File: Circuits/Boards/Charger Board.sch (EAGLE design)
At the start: 0 parts

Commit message: 
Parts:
- added B1: PIEZOBUZZER, Passive:PIEZOBUZZER
- added C1, C3, C8, C9: 1uf, Passive:CAP0603
- added C2, C6, C7: 10uf, Passive:CAP0805
- added C4, C5: 4.7uf, Passive:CAP0603
- added CON1: ISP(2X3), Mechanical:ISP(2X3)
- added CON2: FTDI(1X6), Mechanical:FTDI(1X6)
- added LED1, LED10, LED8, LED9: (no value), Passive:LED0603
- added LED13, LED2, LED3, LED4, LED5, LED6, LED7: IR, Passive:LED5MMRA
- added PR1: 500k-20k, Passive:CDSPHOTORESISTOR
- added R1: 2k, Passive:RES0603
- added R10, R11, R12, R13, R14, R15, R17, R18, R19, R20, R21, R22, R24, R25, R26, R27, R28: (no value), Passive:RES0603
- added R16, R23: 500, Passive:RES0603
- added R2: 1.5k, Passive:RES0603
- added R3: 400, Passive:RES0603
- added R4: 600, Passive:RES0603
- added R5, R7: 10k, Passive:RES0603
- added R6: 15k, Passive:RES0603
- added R8: 1k, Passive:RES0603
- added R9: 20k, Passive:RES0603
- added T1, T2, T3: NPN2N2222, Passive:NPN2N2222
- added T4, T5, T6, T7, T8, T9: TEFT4300, Passive:TEFT4300
- added U1: ATMEGA324P, DigitalIC:ATMEGA324P
- added U2: MCP73832SOT-23, PowerIC:MCP73832SOT-23
- added U3: TB6552FN/FNG, DigitalIC:TB6552FN/FNG
- added V1: MCP1700-3002E, PowerIC:MCP1700-3002E
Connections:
- new net +3V: B1.+, C2.1, C3.1, C6.1, C7.1, C8.1, LED13.A, LED2.A, LED3.A, LED4.A, LED5.A, LED6.A, LED7.A, LED9.A, PR1.2, R7.1, R8.2, T4.C, T5.C, T6.C, T7.C, T8.C, T9.C, U1.AREF, U1.AVCC, U1.VCC, U3.VCC, V1.OUT
- new net +VBAT: C1.1, C4.1, C9.1, R5.2, U2.VBAT, U3.VM, V1.IN
- new net +VCHG: C5.1, R2.2, R3.2, U2.VDD
- new net AIN1: U3.AIN1
- new net AIN2: U3.AIN2
- new net APWM: U3.APWM
- new net BIN1: U3.BIN1
- new net BIN2: U3.BIN2
- new net BPWM: U3.BPWM
- new net BUZZER: R28.1
- new net CHGDETECT: R3.1, R4.2
- new net CHGSTATUS: LED1.C, U2.STAT
- new net DISTANCELED: R23.1
- new net GND: C1.2, C2.2, C3.2, C4.2, C5.2, C6.2, C7.2, C8.2, CON1.GND, CON2.GND, R1.1, R17.1, R18.1, R19.1, R20.1, R21.1, R24.1, R4.1, R6.1, R9.1, T1.E, T2.E, T3.E, U1.GND, U2.VSS, U3.GND, U3.PGND, V1.GND
- new net LED1: R25.1
- new net LED2: R26.1
- new net LED3: R27.1
- new net LIGHTSENSE: PR1.1, R9.2, U1.PA1(ADC1/PCINT1)
- new net LINESENSE1: U1.PA2(ADC2/PCINT2)
- new net LINESENSE2: U1.PA3(ADC3/PCINT3)
- new net MA+: U3.AO1
- new net MA-: U3.AO2
- new net MB+: U3.BO1
- new net MB-: U3.BO2
- new net N$1: R1.2, U2.PROG
- new net N$10: R10.1, R11.1, R12.1, R13.1, R14.1, R15.1, T2.C
- new net N$11: R16.2, T2.B
- new net N$12: R22.1, T3.C
- new net N$13: LED2.C, R10.2
- new net N$14: LED3.C, R11.2
- new net N$15: LED4.C, R12.2
- new net N$16: LED5.C, R13.2
- new net N$17: LED6.C, R14.2
- new net N$18: LED7.C, R15.2
- new net N$19: R23.2, T3.B
- new net N$2: CON1.MOSI, U1.PB5(PCINT13/MOSI)
- new net N$20: LED8.C, R25.2
- new net N$21: LED9.C, R26.2
- new net N$22: LED10.C, R27.2
- new net N$23: C9.2
- new net N$24: LED10.A, LED8.A
- new net N$25: LED13.C, R22.2
- new net N$26: R28.2, T1.B
- new net N$3: CON1.MISO, U1.PB6(PCINT14/MISO)
- new net N$4: LED1.A, R2.1
- new net N$5: CON1.SCK, U1.PB7(PCINT15/SCK)
- new net N$6: CON1.!RESET, R7.2, U1.!RESET
- new net N$7: CON2.RXI, U1.PD1(PCINT25/TXD0)
- new net N$8: CON2.TXO, U1.PD0(PCINT24/RXD0)
- new net N$9: B1.-, R8.1, T1.C
- new net R_A: R17.2, T4.E
- new net R_D: R18.2, R19.2, R20.2, R21.2, R24.2, T5.E, T6.E, T7.E, T8.E, T9.E
- new net STBY: U3.ASTBY, U3.BSTBY
- new net TRANSMITLEDS: R16.1
- new net VSENSE: R5.1, R6.2, U1.PA0(ADC0/PCINT0)
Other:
- note added: "4.6v ideal"

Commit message: 
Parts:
- removed C1, C8, C9: 1uf, Passive:CAP0603
- removed C2, C7: 10uf, Passive:CAP0805
- removed C4, C5: 4.7uf, Passive:CAP0603
- removed LED1: (no value), Passive:LED0603
- removed LED13: IR, Passive:LED5MMRA
- removed PR1: 500k-20k, Passive:CDSPHOTORESISTOR
- removed R1: 2k, Passive:RES0603
- removed R2: 1.5k, Passive:RES0603
- removed R22: (no value), Passive:RES0603
- removed R23: 500, Passive:RES0603
- removed R3: 400, Passive:RES0603
- removed R4: 600, Passive:RES0603
- removed R5: 10k, Passive:RES0603
- removed R6: 15k, Passive:RES0603
- removed R9: 20k, Passive:RES0603
- removed T3: NPN2N2222, Passive:NPN2N2222
- removed U2: MCP73832SOT-23, PowerIC:MCP73832SOT-23
- removed U3: TB6552FN/FNG, DigitalIC:TB6552FN/FNG
- removed V1: MCP1700-3002E, PowerIC:MCP1700-3002E
- added CON3: CHARGERCONTACTS, Mechanical:CHARGERCONTACTS
- added S1: ROCKER_SWITCH, Mechanical:ROCKER_SWITCH
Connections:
- removed net +VBAT: C1.1, C4.1, C9.1, R5.2, U2.VBAT, U3.VM, V1.IN
- removed net +VCHG: C5.1, R2.2, R3.2, U2.VDD
- removed net AIN1: U3.AIN1
- removed net AIN2: U3.AIN2
- removed net APWM: U3.APWM
- removed net BIN1: U3.BIN1
- removed net BIN2: U3.BIN2
- removed net BPWM: U3.BPWM
- removed net CHGDETECT: R3.1, R4.2
- removed net CHGSTATUS: LED1.C, U2.STAT
- removed net DISTANCELED: R23.1
- removed net LIGHTSENSE: PR1.1, R9.2, U1.PA1(ADC1/PCINT1)
- removed net LINESENSE1: U1.PA2(ADC2/PCINT2)
- removed net LINESENSE2: U1.PA3(ADC3/PCINT3)
- removed net MA+: U3.AO1
- removed net MA-: U3.AO2
- removed net MB+: U3.BO1
- removed net MB-: U3.BO2
- removed net N$1: R1.2, U2.PROG
- removed net N$12: R22.1, T3.C
- removed net N$19: R23.2, T3.B
- removed net N$23: C9.2
- removed net N$25: LED13.C, R22.2
- removed net STBY: U3.ASTBY, U3.BSTBY
- removed net VSENSE: R5.1, R6.2, U1.PA0(ADC0/PCINT0)
- new net +5V: B1.+, C3.1, C6.1, LED2.A, LED3.A, LED4.A, LED5.A, LED6.A, LED7.A, LED9.A, R8.2, S1.2, T4.C, T5.C, T6.C, T7.C, T8.C, T9.C, U1.AREF, U1.AVCC, U1.VCC
- new net CURRENTSENSE: U1.PA0(ADC0/PCINT0)
- new net VIN: S1.1
- net +3V: no longer B1.+, C2.1, C3.1, C6.1, C7.1, C8.1, LED13.A, LED2.A, LED3.A, LED4.A, LED5.A, LED6.A, LED7.A, LED9.A, PR1.2, R8.2, T4.C, T5.C, T6.C, T7.C, T8.C, T9.C, U1.AREF, U1.AVCC, U1.VCC, U3.VCC, V1.OUT
- net GND: now also CON3.GND; no longer C1.2, C2.2, C4.2, C5.2, C7.2, C8.2, R1.1, R4.1, R6.1, R9.1, T3.E, U2.VSS, U3.GND, U3.PGND, V1.GND
- net N$4: now also CON3.+V; no longer LED1.A, R2.1
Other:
- note removed: "4.6v ideal"
- moved on the sheet: C6, LED2, LED3, LED4, LED5, LED6, LED7, R10, R11, R12, R13, R14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

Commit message: updated charger schematic, and added swarm board board file
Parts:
- added C1: .1uf, Passive:CAP0603
- added C2: 1nf, Passive:CAP0603
- added R1: 1k, Passive:RES0603
- added T3: IRF7416PBF, Passive:IRF7416PBF
- added U2: ACS711, PowerIC:ACS711
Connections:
- removed net +3V: R7.1
- new net +VCHG: B1.+, C1.1, C3.1, LED9.A, R7.1, R8.2, S1.2, T3.S, U1.AREF, U1.AVCC, U1.VCC, U2.VCC
- new net CHARGER: T3.G, U1.PB0(XCK0/T0/PCINT8)
- new net N$1: T3.D, U2.IP+
- new net N$12: C2.1, R1.1, U2.VIOUT
- net +5V: no longer B1.+, C3.1, LED9.A, R8.2, S1.2, U1.AREF, U1.AVCC, U1.VCC
- net CURRENTSENSE: now also R1.2
- net GND: now also C2.2, U2.GND
- net N$4: now also U2.IP-
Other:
- note added: "These go to the charger contacts"

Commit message: Large updates to the charger board
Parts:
- added C4: .1uf, Passive:CAP0603
- added C5: 1uf, Passive:CAP0603
- added D1, D2: PMEG3050EP, Passive:PMEG3050EP
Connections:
- removed net N$4: CON3.+V, U2.IP-
- new net N$19: CON3.+V, D1.C, D2.C
- new net N$23: D1.A, D2.A, U2.IP-
- net +5V: now also B1.+, C1.1, C3.1, C4.1, C5.1, LED9.A, R8.2, S1.2, T3.S, U1.AREF, U1.AVCC, U1.VCC, U2.VCC
- net +VCHG: no longer B1.+, C1.1, C3.1, LED9.A, R8.2, S1.2, T3.S, U1.AREF, U1.AVCC, U1.VCC, U2.VCC
- net GND: now also C1.2, C4.2, C5.2
- net LED1: now also U1.PB1(T1/CLKO/PCINT9)
- net LED2: now also U1.PB2(AIN0/INT2/PCINT10)
- net LED3: now also U1.PB3(AIN1/OC0A/PCINT11)
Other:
- moved on the sheet: B1, C1, C2, LED10, LED8, LED9, R1, R25, R26, R27, R28, R8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

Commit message: updates to both boards and libraries. Added hall effect sensors to charger board
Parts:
- added U10, U3, U4, U5, U6, U7, U8, U9: HALLEFFECT, DigitalIC:HALLEFFECT
- R25, R26, R27: value (none) -> 200
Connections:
- new net BAY1: U1.PC0(PCINT16/SCL), U3.!VOUT
- new net BAY2: U1.PC1(PCINT17/SDA), U4.!VOUT
- new net BAY3: U1.PC2(PCINT18/TCK), U5.!VOUT
- new net BAY4: U1.PC3(PCINT19/TMS), U6.!VOUT
- new net BAY5: U1.PC4(TDO/PCINT20), U7.!VOUT
- new net BAY6: U1.PC5(TDI/PCINT21), U8.!VOUT
- new net BAY7: U1.PC6(TOSC1/PCINT22), U9.!VOUT
- new net BAY8: U1.PC7(TOSC2/PCINT23), U10.!VOUT
- net +5V: now also U10.VCC, U3.VCC, U4.VCC, U5.VCC, U6.VCC, U7.VCC, U8.VCC, U9.VCC
- net GND: now also U10.GND, U3.GND, U4.GND, U5.GND, U6.GND, U7.GND, U8.GND, U9.GND
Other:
- moved on the sheet: C6, CON2, LED2, LED3, LED4, LED5, LED6, LED7, R10, R11, R12, R13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

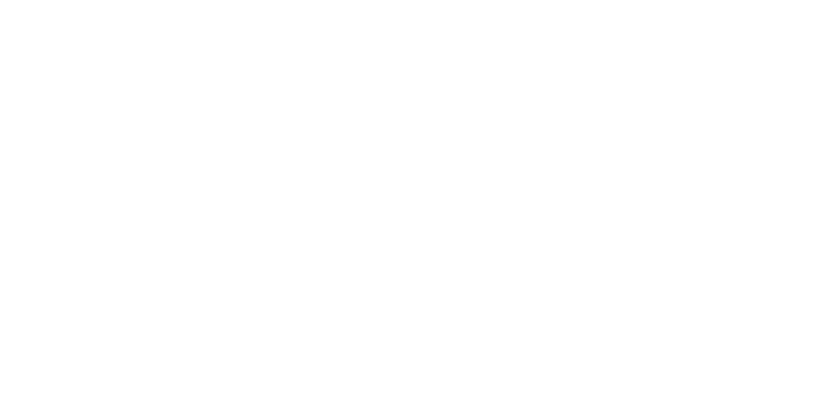
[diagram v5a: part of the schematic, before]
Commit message: 
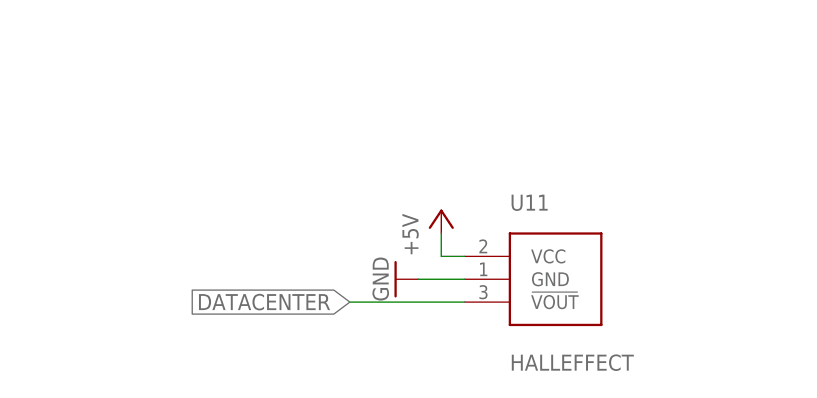
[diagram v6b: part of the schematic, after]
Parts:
- added U11: HALLEFFECT, DigitalIC:HALLEFFECT
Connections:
- new net DATACENTER: U11.!VOUT
- net +5V: now also U11.VCC
- net GND: now also U11.GND
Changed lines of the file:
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@@
 <part name="P+17" library="Supply" deviceset="+5V" device=""/>
 <part name="U10" library="DigitalIC" deviceset="HALLEFFECT" device=""/>
+<part name="GND24" library="Supply" deviceset="GND" device=""/>
+<part name="P+18" library="Supply" deviceset="+5V" device=""/>
+<part name="U11" library="DigitalIC" deviceset="HALLEFFECT" device=""/>
 </parts>
 <sheets>
@@
 <instance part="P+17" gate="1" x="162.56" y="-106.68"/>
 <instance part="U10" gate="G$1" x="175.26" y="-114.3"/>
+<instance part="GND24" gate="1" x="154.94" y="-162.56" rot="R270"/>
+<instance part="P+18" gate="1" x="160.02" y="-154.94"/>
+<instance part="U11" gate="G$1" x="172.72" y="-162.56"/>
 </instances>
 <busses>
@@
 <pinref part="GND23" gate="1" pin="GND"/>
 <pinref part="U10" gate="G$1" pin="GND"/>
+</segment>
+<segment>
+<wire x1="162.56" y1="-162.56" x2="157.48" y2="-162.56" width="0.1524" layer="91"/>
+<pinref part="GND24" gate="1" pin="GND"/>
+<pinref part="U11" gate="G$1" pin="GND"/>
 </segment>
 </net>
@@
 <pinref part="U10" gate="G$1" pin="VCC"/>
 </segment>
+<segment>
+<wire x1="162.56" y1="-160.02" x2="160.02" y2="-160.02" width="0.1524" layer="91"/>
+<wire x1="160.02" y1="-160.02" x2="160.02" y2="-157.48" width="0.1524" layer="91"/>
+<pinref part="P+18" gate="1" pin="+5V"/>
+<pinref part="U11" gate="G$1" pin="VCC"/>
+</segment>
 </net>
 <net name="VIN" class="0">
@@
 </segment>
 </net>
+<net name="DATACENTER" class="0">
+<segment>
+<wire x1="162.56" y1="-165.1" x2="149.86" y2="-165.1" width="0.1524" layer="91"/>
+<label x="149.86" y="-165.1" size="1.778" layer="91" rot="R180" xref="yes"/>
+<pinref part="U11" gate="G$1" pin="!VOUT"/>
+</segment>
+</net>

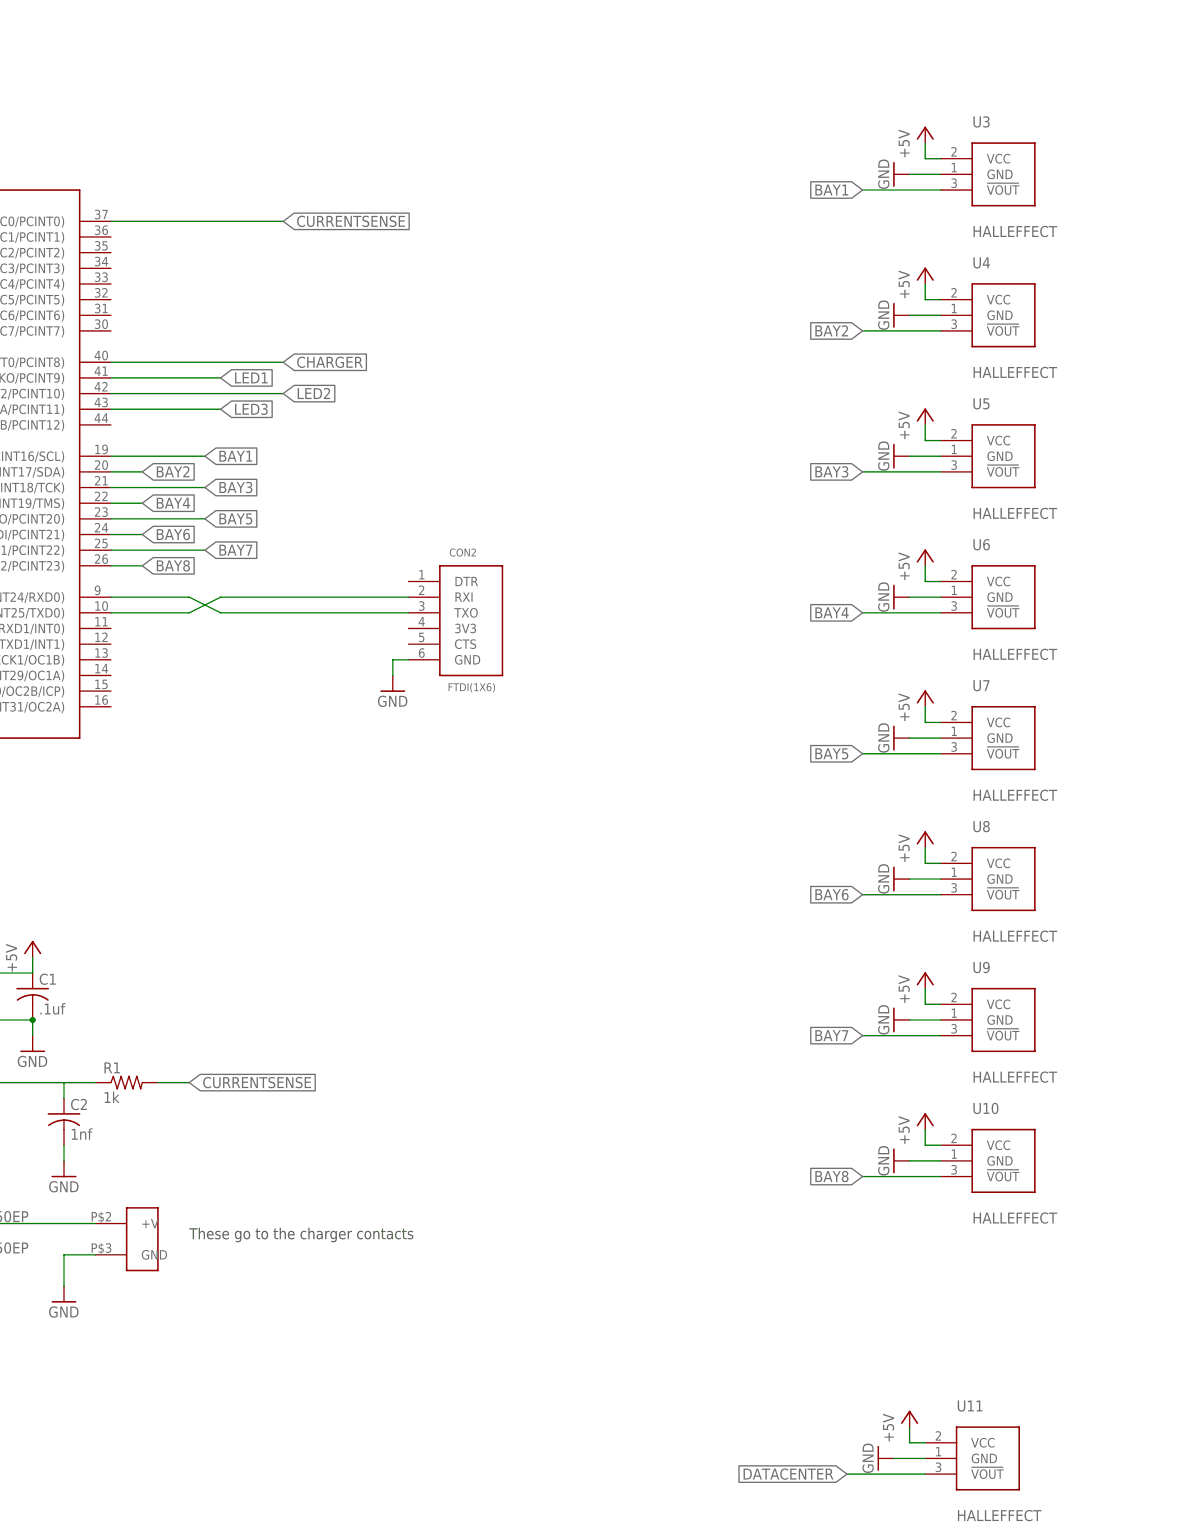
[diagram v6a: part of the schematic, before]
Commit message: 
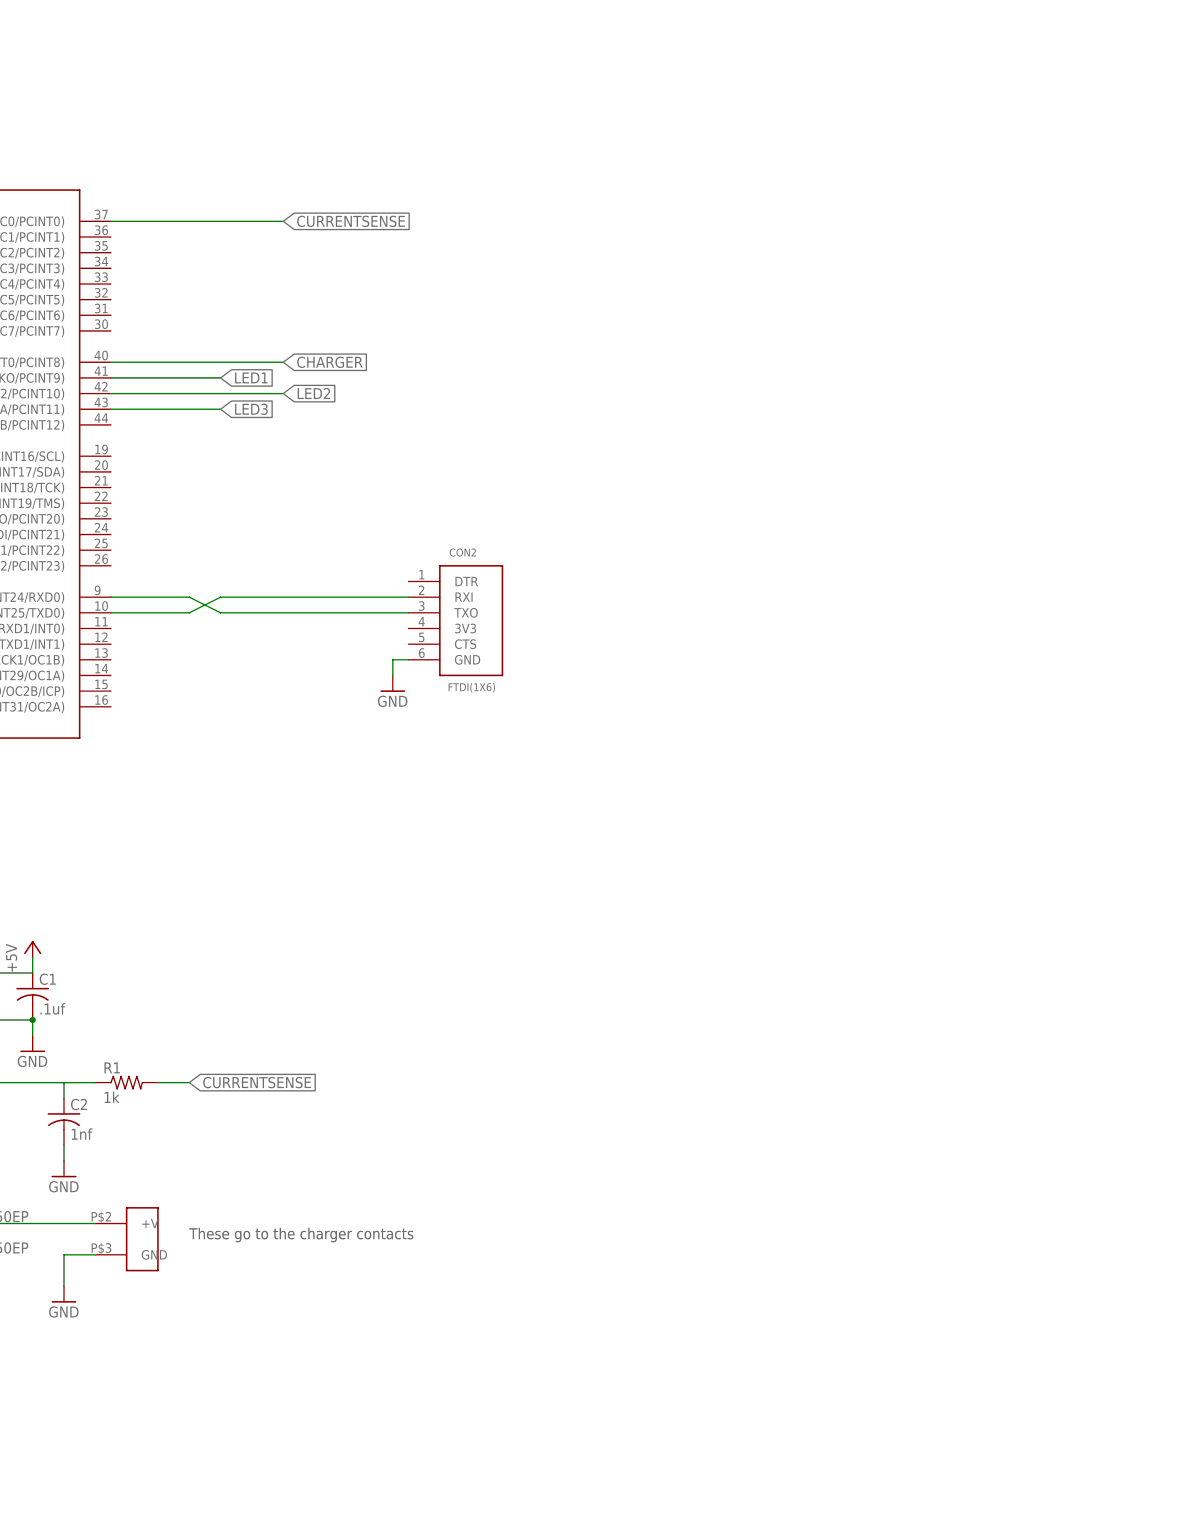
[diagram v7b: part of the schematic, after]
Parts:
- removed U10, U11, U3, U4, U5, U6, U7, U8, U9: HALLEFFECT, DigitalIC:HALLEFFECT
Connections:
- removed net BAY1: U1.PC0(PCINT16/SCL), U3.!VOUT
- removed net BAY2: U1.PC1(PCINT17/SDA), U4.!VOUT
- removed net BAY3: U1.PC2(PCINT18/TCK), U5.!VOUT
- removed net BAY4: U1.PC3(PCINT19/TMS), U6.!VOUT
- removed net BAY5: U1.PC4(TDO/PCINT20), U7.!VOUT
- removed net BAY6: U1.PC5(TDI/PCINT21), U8.!VOUT
- removed net BAY7: U1.PC6(TOSC1/PCINT22), U9.!VOUT
- removed net BAY8: U1.PC7(TOSC2/PCINT23), U10.!VOUT
- removed net DATACENTER: U11.!VOUT
- net +5V: no longer U10.VCC, U11.VCC, U3.VCC, U4.VCC, U5.VCC, U6.VCC, U7.VCC, U8.VCC, U9.VCC
- net GND: no longer U10.GND, U11.GND, U3.GND, U4.GND, U5.GND, U6.GND, U7.GND, U8.GND, U9.GND

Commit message: updated libraries and charger board
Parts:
- removed CON2: FTDI(1X6), Mechanical:FTDI(1X6)
- removed D1, D2: PMEG3050EP, Passive:PMEG3050EP
- removed R21, R24: (no value), Passive:RES0603
- removed T4, T5, T6, T7, T8, T9: TEFT4300, Passive:TEFT4300
- added CON10, CON11, CON12, CON4, CON5, CON6, CON7, CON8, CON9: HEADER_3X1, Mechanical:HEADER_3X1
- added IC1: NCP1117DT33G, PowerIC:NCP1117DT33G
- added R2, R3, R4, R5, R6, R9: 100, Passive:RES0603
- added U$1, U$2: FTDI_3PIN, Mechanical:FTDI_3PIN
- added U$3, U$4: MBRS410LT3, Passive:MBRS410LT3
- C4: value .1uf -> 10uf; device Passive:CAP0603 -> Passive:CAP0805
- C5: value 1uf -> 10uf; device Passive:CAP0603 -> Passive:CAP0805
- CON3: value CHARGERCONTACTS -> HEADER_3X1; device Mechanical:CHARGERCONTACTS -> Mechanical:HEADER_3X1
- R17, R18, R19, R20: value (none) -> 100
- T3: value IRF7416PBF -> SI4421DY; device Passive:IRF7416PBF -> Passive:SI4421DY
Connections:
- removed net +VCHG: R7.1
- removed net R_A: R17.2, T4.E
- removed net R_D: R18.2, R19.2, R20.2, R21.2, R24.2, T5.E, T6.E, T7.E, T8.E, T9.E
- removed net VIN: S1.1
- new net +3V3: B1.+, C1.1, C3.1, C5.1, C6.1, IC1.OUT, LED2.A, LED3.A, LED4.A, LED5.A, LED6.A, LED7.A, LED9.A, R7.1, R8.2, U1.AREF, U1.AVCC, U1.VCC, U2.VCC
- new net CHARGE+: CON10.2, CON11.2, CON12.2, CON3.2, CON4.2, CON5.2, CON6.2, CON7.2, CON8.2, CON9.2, U$3.C, U$4.C
- new net N$25: C4.1, IC1.IN, S1.2
- new net N$27: CON3.1, R2.2
- new net N$28: CON4.1, R3.2
- new net N$29: CON5.1, R4.2
- new net N$39: CON6.1, R5.2
- new net N$4: U$2.TXO, U1.PD2(PCINT26/RXD1/INT0)
- new net N$40: CON7.1, R6.2
- new net N$41: CON8.1, R9.2
- new net N$42: CON9.1, R17.2
- new net N$43: CON10.1, R18.2
- new net N$44: CON11.1, R19.2
- new net N$45: CON12.1, R20.2
- new net SECTION1: R2.1
- new net SECTION10: R20.1
- new net SECTION2: R3.1
- new net SECTION3: R4.1
- new net SECTION4: R5.1
- new net SECTION5: R6.1
- new net SECTION6: R9.1
- new net SECTION7: R17.1
- new net SECTION8: R18.1
- new net SECTION9: R19.1
- net +5V: now also S1.1; no longer B1.+, C1.1, C3.1, C4.1, C5.1, C6.1, LED2.A, LED3.A, LED4.A, LED5.A, LED6.A, LED7.A, LED9.A, R8.2, S1.2, T4.C, T5.C, T6.C, T7.C, T8.C, T9.C, U1.AREF, U1.AVCC, U1.VCC, U2.VCC
- net GND: now also CON10.3, CON11.3, CON12.3, CON3.3, CON4.3, CON5.3, CON6.3, CON7.3, CON8.3, CON9.3, IC1.GND, U$1.GND, U$2.GND; no longer CON2.GND, CON3.GND, R17.1, R18.1, R19.1, R20.1, R21.1, R24.1
- net N$19: now also U$2.RXI, U1.PD3(PCINT27/TXD1/INT1); no longer CON3.+V, D1.C, D2.C
- net N$23: now also U$3.A, U$4.A; no longer D1.A, D2.A
- net N$7: now also U$1.RXI; no longer CON2.RXI
- net N$8: now also U$1.TXO; no longer CON2.TXO
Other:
- moved on the sheet: C3, C4, C5, C6, LED2, LED3, LED4, LED5, LED6, LED7, R10, R11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
